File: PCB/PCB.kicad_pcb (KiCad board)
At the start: 2 copper layers, 95.2 x 61 mm, 47 parts, among them J1 Conn_01x02, J2 6P4C, J3 Conn_01x03, J4 Conn_02x08_Odd_Even, J5 Conn_01x08, J6 Conn_01x04, J7 Conn_02x03_Odd_Even, U1 LM358, U2 L293D

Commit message: PCB: Reattach vias to GND
Somewhere in the KiCad upgrade, it seems some vias got attached to
different nets. This manually fixes them.
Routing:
- net unconnected-(A1-~{RESET}-Pad1): vias 2 -> 0
- net unconnected-(A1-D13-Pad25): vias 1 -> 0
- net STRIP8: vias 2 -> 0
- net STRIP3: vias 1 -> 0
- net SCL: vias 1 -> 0
- net MOTION: vias 1 -> 0
- net GND: vias 102 -> 111
- net BRIDGE_IN_2: vias 1 -> 0
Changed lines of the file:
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@@
+	)
+	(via
+		(at 62.865 182.88)
+		(size 0.8)
+		(drill 0.4)
+		(layers "F.Cu" "B.Cu")
+		(net 3)
 	)
 	(via
@@
 	)
 	(via
+		(at 64.135 184.15)
+		(size 0.8)
+		(drill 0.4)
+		(layers "F.Cu" "B.Cu")
+		(net 3)
+	)
+	(via
 		(at 61.595 177.8)
 		(size 0.8)
@@
 	)
 	(via
+		(at 73.66 154.305)
+		(size 0.8)
+		(drill 0.4)
+		(layers "F.Cu" "B.Cu")
+		(free yes)
+		(net 3)
+	)
+	(via
 		(at 71.755 132.715)
 		(size 0.8)
@@
 	)
 	(via
+		(at 64.135 175.26)
+		(size 0.8)
+		(drill 0.4)
+		(layers "F.Cu" "B.Cu")
+		(net 3)
+	)
+	(via
 		(at 96.52 132.715)
 		(size 0.8)
@@
 	)
 	(via
+		(at 60.325 160.02)
+		(size 0.8)
+		(drill 0.4)
+		(layers "F.Cu" "B.Cu")
+		(net 3)
+	)
+	(via
 		(at 105.41 132.715)
 		(size 0.8)
@@
 	)
 	(via
+		(at 79.375 174.625)
+		(size 0.8)
+		(drill 0.4)
+		(layers "F.Cu" "B.Cu")
+		(net 3)
+	)
+	(via
 		(at 137.795 181.61)
 		(size 0.8)
@@
 	)
 	(via
+		(at 95.885 189.865)
+		(size 0.8)
+		(drill 0.4)
+		(layers "F.Cu" "B.Cu")
+		(net 3)
+	)
+	(via
 		(at 144.145 144.145)
 		(size 0.8)
@@
 	)
 	(via
+		(at 127.635 135.89)
+		(size 0.8)
+		(drill 0.4)
+		(layers "F.Cu" "B.Cu")
+		(net 3)
+	)
+	(via
 		(at 127.635 147.32)
 		(size 0.8)
@@
 	(via
 		(at 135.89 163.195)
+		(size 0.8)
+		(drill 0.4)
+		(layers "F.Cu" "B.Cu")
+		(net 3)
+	)
+	(via
+		(at 132.715 135.89)
 		(size 0.8)
 		(drill 0.4)
@@
 		(net 8)
 	)
-	(via
-		(at 79.375 174.625)
-		(size 0.8)
-		(drill 0.4)
-		(layers "F.Cu" "B.Cu")
-		(net 9)
-	)
 	(segment
 		(start 106.68 156.19)
@@
 		(net 10)
 	)
-	(via
-		(at 64.135 175.26)
-		(size 0.8)
-		(drill 0.4)
-		(layers "F.Cu" "B.Cu")
-		(net 10)
-	)
 	(segment
 		(start 113.03 178.64)
@@
 		(net 16)
 	)
-	(via
-		(at 127.635 135.89)
-		(size 0.8)
-		(drill 0.4)
-		(layers "F.Cu" "B.Cu")
-		(net 16)
-	)
-	(via
-		(at 62.865 182.88)
-		(size 0.8)
-		(drill 0.4)
-		(layers "F.Cu" "B.Cu")
-		(net 17)
-	)
-	(via
-		(at 64.135 184.15)
-		(size 0.8)
-		(drill 0.4)
-		(layers "F.Cu" "B.Cu")
-		(net 17)
-	)
 	(segment
 		(start 117.24 165.1)
@@
 		(net 35)
 	)
-	(via
-		(at 132.715 135.89)
-		(size 0.8)
-		(drill 0.4)
-		(layers "F.Cu" "B.Cu")
-		(net 35)
-	)
 	(segment
 		(start 76.2 182.88)
@@
 		(net 38)
 	)
-	(via
-		(at 73.66 154.305)
-		(size 0.8)
-		(drill 0.4)
-		(layers "F.Cu" "B.Cu")
-		(net 38)
-	)
 	(segment
 		(start 83.82 182.88)
@@
 		(net 43)
 	)
-	(via
-		(at 60.325 160.02)
-		(size 0.8)
-		(drill 0.4)
-		(layers "F.Cu" "B.Cu")
-		(net 43)
-	)
-	(via
-		(at 95.885 189.865)
-		(size 0.8)
-		(drill 0.4)
-		(layers "F.Cu" "B.Cu")
-		(net 43)
-	)

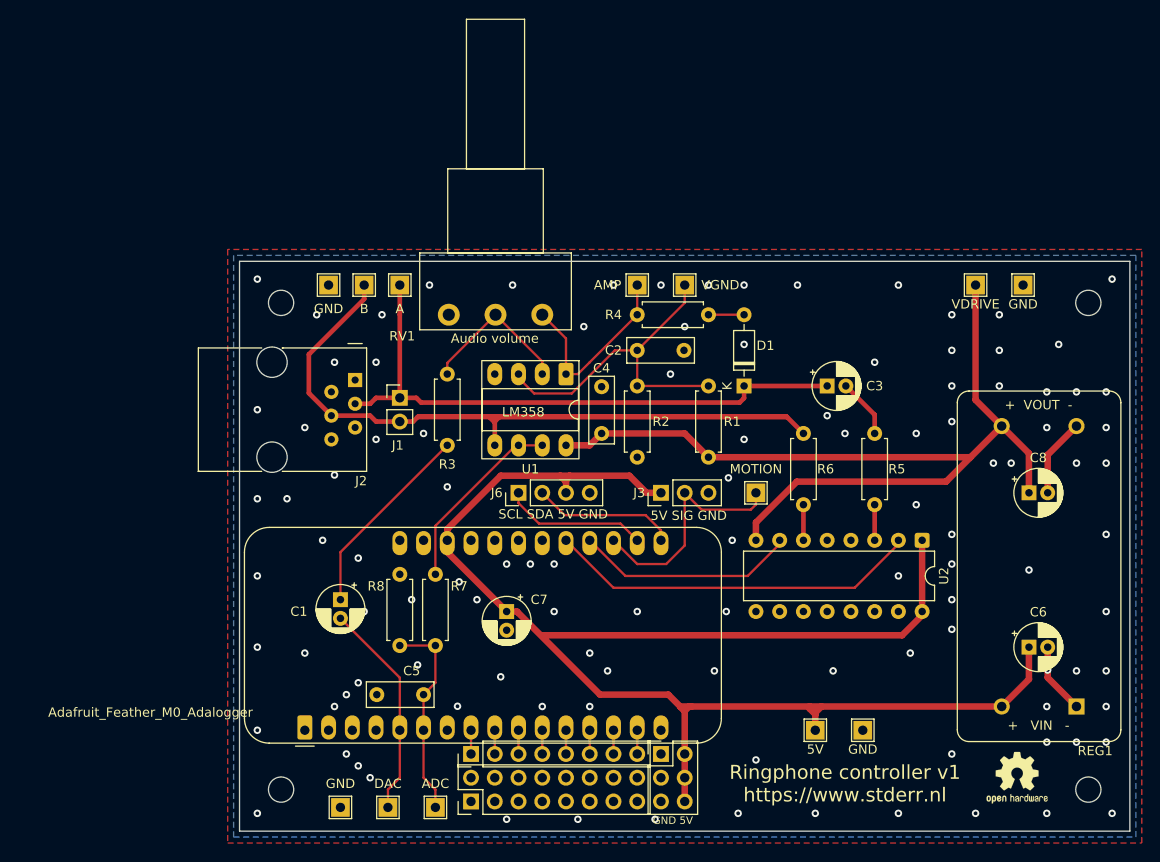
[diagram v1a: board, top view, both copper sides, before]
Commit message: PCB: Fix DRC errors
This updates a footprint, makes small layout changes and ignores some
violations.
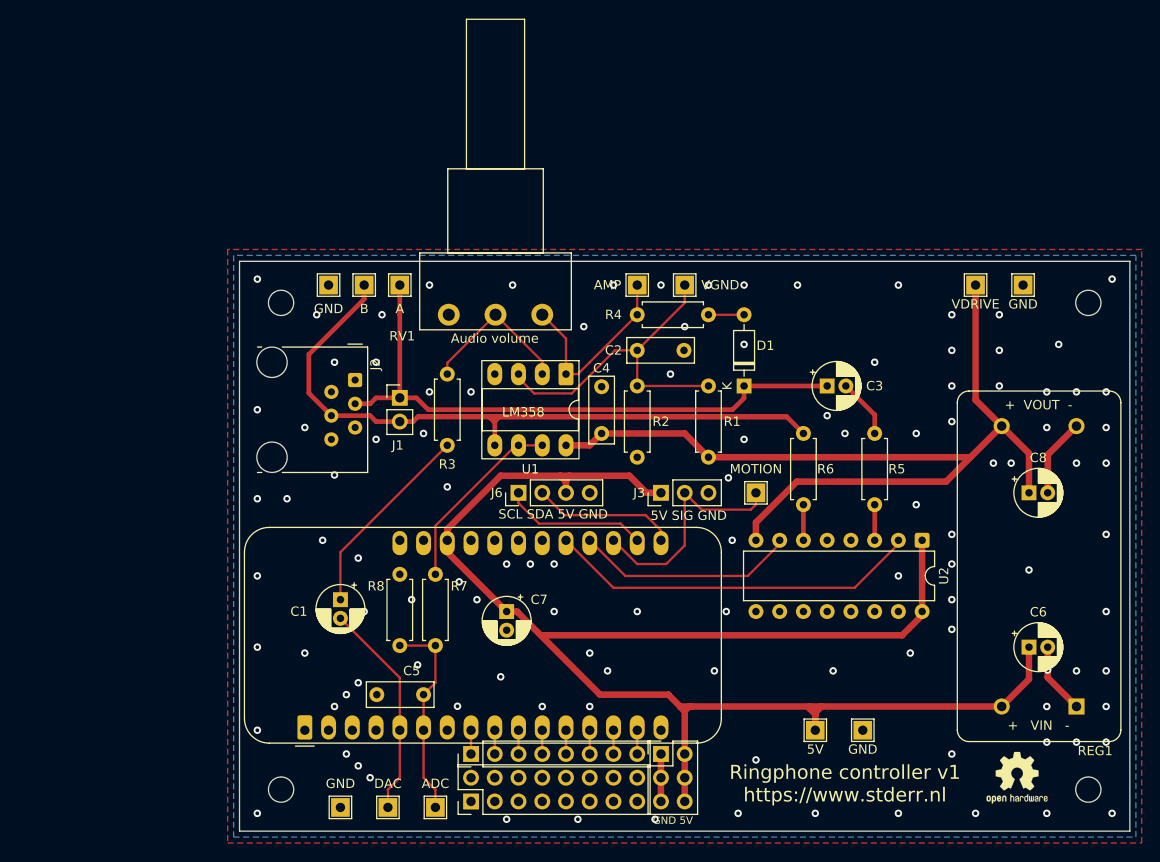
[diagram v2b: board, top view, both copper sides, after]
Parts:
- J2: footprint Connector_RJ:RJ12_Amphenol_54601 -> Connector_RJ:RJ12_Amphenol_54601-x06_Horizontal
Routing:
- net GND: track 16.0 -> 21.1 mm, vias 111 -> 113
- net TELEPHONE_A: track 64.5 -> 65.2 mm
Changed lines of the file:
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@@
 		)
 	)
-	(footprint "Connector_RJ:RJ12_Amphenol_54601"
+	(footprint "Connector_RJ:RJ12_Amphenol_54601-x06_Horizontal"
 		(layer "F.Cu")
 		(at 63.8 142.875 -90)
-		(descr "RJ12 connector  https://cdn.amphenol-icc.com/media/wysiwyg/files/drawing/c-bmj-0082.pdf")
+		(descr "RJ12 6P6C horizontal socket, plastic body, tab down, https://cdn.amphenol-icc.com/media/wysiwyg/files/drawing/c-bmj-0082.pdf")
 		(tags "RJ12 connector")
 		(property "Reference" "J2"
-			(at 10.795 -0.6398 180)
+			(at -1.66 -2.16 90)
 			(layer "F.SilkS")
 			(effects
@@
 		)
 		(property "Value" "6P4C"
-			(at 4.445 8.555 180)
+			(at 3.55 18.3 90)
 			(layer "F.Fab")
 			(effects
@@
 		(property "Datasheet" ""
 			(at 0 0 270)
+			(unlocked yes)
 			(layer "F.Fab")
 			(hide yes)
@@
 			)
 		)
-		(property "Description" "RJ connector, 6P6C (6 positions 6 connected), RJ12/RJ18/RJ25"
+		(property "Description" ""
 			(at 0 0 270)
+			(unlocked yes)
 			(layer "F.Fab")
 			(hide yes)
@@
 		(attr through_hole)
 		(fp_line
-			(start -3.43 16.77)
-			(end -3.43 9.99)
+			(start -3.53 10.45)
+			(end -3.53 9.99)
 			(stroke
 				(width 0.12)
@@
 		)
 		(fp_line
-			(start 9.77 16.77)
-			(end -3.43 16.77)
+			(start 9.89 10.45)
+			(end 9.89 9.99)
 			(stroke
 				(width 0.12)
@@
 		)
 		(fp_line
-			(start 9.77 16.77)
-			(end 9.77 9.99)
+			(start -3.53 7.79)
+			(end -3.53 -1.34)
 			(stroke
 				(width 0.12)
@@
 		)
 		(fp_line
-			(start 9.77 16.76)
-			(end 9.77 16.77)
+			(start -3.84 0.77)
+			(end -3.84 -0.76)
 			(stroke
-				(width 0.1)
+				(width 0.12)
 				(type solid)
 			)
@@
 		)
 		(fp_line
-			(start 9.77 16.65)
-			(end 9.77 16.77)
+			(start -3.53 -1.34)
+			(end 9.89 -1.34)
 			(stroke
-				(width 0.1)
+				(width 0.12)
 				(type solid)
 			)
@@
 		)
 		(fp_line
-			(start -3.43 7.79)
-			(end -3.43 -1.23)
+			(start 9.89 -1.34)
+			(end 9.89 7.79)
 			(stroke
 				(width 0.12)
@@
 		)
 		(fp_line
-			(start -3.43 7.72)
-			(end -3.43 7.79)
+			(start 10.28 17.27)
+			(end -3.92 17.27)
 			(stroke
-				(width 0.1)
+				(width 0.05)
 				(type solid)
 			)
-			(layer "F.SilkS")
+			(layer "F.CrtYd")
 		)
 		(fp_line
-			(start -3.9 0.77)
-			(end -3.9 -0.76)
+			(start -4.03 9.64)
+			(end -3.92 9.64)
 			(stroke
-				(width 0.12)
-				(type solid)
+				(width 0.05)
+				(type default)
 			)
-			(layer "F.SilkS")
+			(layer "F.CrtYd")
 		)
 		(fp_line
-			(start -3.43 -1.23)
-			(end 9.77 -1.23)
+			(start -3.92 9.64)
+			(end -3.92 17.27)
 			(stroke
-				(width 0.12)
+				(width 0.05)
 				(type solid)
 			)
-			(layer "F.SilkS")
+			(layer "F.CrtYd")
 		)
 		(fp_line
-			(start 9.77 -1.23)
-			(end 9.77 7.79)
+			(start 10.28 9.64)
+			(end 10.28 17.27)
 			(stroke
-				(width 0.12)
+				(width 0.05)
 				(type solid)
 			)
-			(layer "F.SilkS")
+			(layer "F.CrtYd")
 		)
 		(fp_line
-			(start -4.04 17.27)
-			(end -4.04 -1.73)
+			(start 10.39 9.64)
+			(end 10.28 9.64)
 			(stroke
 				(width 0.05)
-				(type solid)
+				(type default)
+			)
+			(layer "F.CrtYd")
+		)
+		(fp_line
+			(start -4.03 8.14)
+			(end -4.03 9.64)
+			(stroke
+				(width 0.05)
+				(type default)
+			)
+			(layer "F.CrtYd")
+		)
+		(fp_line
+			(start -4.03 8.14)
+			(end -3.92 8.14)
+			(stroke
+				(width 0.05)
+				(type default)
 			)
 			(layer "F.CrtYd")
 		)
 		(fp_line
-			(start 10.38 17.27)
-			(end -4.04 17.27)
+			(start 10.39 8.14)
+			(end 10.39 9.64)
+			(stroke
+				(width 0.05)
+				(type default)
+			)
+			(layer "F.CrtYd")
+		)
+		(fp_line
+			(start 10.39 8.14)
+			(end 10.28 8.14)
+			(stroke
+				(width 0.05)
+				(type default)
+			)
+			(layer "F.CrtYd")
+		)
+		(fp_line
+			(start -3.92 -1.73)
+			(end -3.92 8.14)
 			(stroke
 				(width 0.05)
@@
 		)
 		(fp_line
-			(start -4.04 -1.73)
-			(end 10.38 -1.73)
+			(start -3.92 -1.73)
+			(end 10.28 -1.73)
 			(stroke
 				(width 0.05)
@@
 		)
 		(fp_line
-			(start 10.38 -1.73)
-			(end 10.38 17.27)
+			(start 10.28 -1.73)
+			(end 10.28 8.14)
 			(stroke
 				(width 0.05)
@@
 		)
 		(fp_line
-			(start -3.43 16.77)
-			(end -3.43 0.52)
+			(start -3.42 16.77)
+			(end -3.42 0.52)
 			(stroke
 				(width 0.1)
@@
 		)
 		(fp_line
-			(start 9.77 16.77)
-			(end -3.43 16.77)
+			(start 9.78 16.77)
+			(end -3.42 16.77)
 			(stroke
 				(width 0.1)
@@
 		)
 		(fp_line
-			(start -3.43 0.52)
-			(end -2.93 0.02)
+			(start -3.42 0.52)
+			(end -2.92 0.02)
 			(stroke
 				(width 0.1)
@@
 		)
 		(fp_line
-			(start -2.93 0.02)
-			(end -3.43 -0.48)
+			(start -2.92 0.02)
+			(end -3.42 -0.48)
 			(stroke
 				(width 0.1)
@@
 		)
 		(fp_line
-			(start -3.43 -0.48)
-			(end -3.43 -1.23)
+			(start -3.42 -0.48)
+			(end -3.42 -1.23)
 			(stroke
 				(width 0.1)
@@
 		)
 		(fp_line
-			(start -3.43 -1.23)
-			(end 9.77 -1.23)
+			(start -3.42 -1.23)
+			(end 9.78 -1.23)
 			(stroke
 				(width 0.1)
@@
 		)
 		(fp_line
-			(start 9.77 -1.23)
-			(end 9.77 16.77)
+			(start 9.78 -1.23)
+			(end 9.78 16.77)
 			(stroke
 				(width 0.1)
@@
 		)
 		(fp_text user "${REFERENCE}"
-			(at 2.54 8.555 180)
+			(at 3.18 7.77 0)
 			(layer "F.Fab")
 			(effects
@@
 		)
 		(pad "" np_thru_hole circle
-			(at -1.91 8.89 270)
+			(at -1.9 8.89 270)
 			(size 3.25 3.25)
 			(drill 3.25)
@@
 		)
 		(pad "" np_thru_hole circle
-			(at 8.25 8.89 270)
+			(at 8.26 8.89 270)
 			(size 3.25 3.25)
 			(drill 3.25)
 			(layers "*.Cu" "*.Mask")
 		)
-		(pad "1" thru_hole rect
+		(pad "1" thru_hole roundrect
 			(at 0 0 270)
 			(size 1.52 1.52)
@@
 			(layers "*.Cu" "*.Mask")
 			(remove_unused_layers no)
+			(roundrect_rratio 0.1644736842)
 			(net 28 "unconnected-(J2-Pad1)")
 			(pintype "passive+no_connect")
@@
 		)
 		(embedded_fonts no)
-		(model "${KISYS3DMOD}/Connector_RJ.3dshapes/RJ12_Amphenol_54601.wrl"
+		(model "${KICAD9_3DMODEL_DIR}/Connector_RJ.3dshapes/RJ12_Amphenol_54601-x06_Horizontal.wrl"
 			(offset
 				(xyz 0 0 0)
@@
 			(at 1.905 -16.51 0)
 			(layer "F.SilkS")
+			(hide yes)
 			(effects
 				(font
@@
 		(sheetname "/")
 		(sheetfile "PCB.kicad_sch")
-		(attr exclude_from_pos_files)
+		(attr exclude_from_pos_files allow_missing_courtyard)
 		(fp_poly
 			(pts
@@
 	)
 	(segment
+		(start 96.52 182.88)
+		(end 96.52 185.42)
+		(width 0.7)
+		(layer "F.Cu")
+		(net 3)
+	)
+	(segment
+		(start 96.52 185.42)
+		(end 96.52 187.96)
+		(width 0.7)
+		(layer "F.Cu")
+		(net 3)
+	)
+	(segment
 		(start 137.89 154.94)
 		(end 137.89 151.504399)
@@
 	)
 	(via
+		(at 71.755 144.145)
+		(size 0.8)
+		(drill 0.4)
+		(layers "F.Cu" "B.Cu")
+		(free yes)
+		(net 3)
+	)
+	(via
 		(at 127.635 143.51)
 		(size 0.8)
@@
 	)
 	(via
+		(at 76.2 144.145)
+		(size 0.8)
+		(drill 0.4)
+		(layers "F.Cu" "B.Cu")
+		(free yes)
+		(net 3)
+	)
+	(via
 		(at 137.795 177.8)
 		(size 0.8)
@@
 	)
 	(segment
-		(start 65.405 145.415)
-		(end 63.8 145.415)
+		(start 104.17 146.05)
+		(end 71.62 146.05)
 		(width 0.5)
 		(layer "F.Cu")
@@
 	)
 	(segment
-		(start 66.04 144.78)
-		(end 65.405 145.415)
+		(start 105.41 143.51)
+		(end 105.41 144.81)
 		(width 0.5)
 		(layer "F.Cu")
@@
 	)
 	(segment
-		(start 104.932 145.288)
-		(end 70.858 145.288)
+		(start 65.405 145.415)
+		(end 63.8 145.415)
 		(width 0.5)
 		(layer "F.Cu")
@@
 	)
 	(segment
-		(start 68.58 135.89)
-		(end 68.58 144.78)
+		(start 66.04 144.78)
+		(end 65.405 145.415)
 		(width 0.5)
 		(layer "F.Cu")
@@
 	)
 	(segment
-		(start 105.41 143.51)
-		(end 105.41 144.81)
+		(start 105.41 144.81)
+		(end 104.17 146.05)
 		(width 0.5)
 		(layer "F.Cu")
@@
 	)
 	(segment
-		(start 114.3 143.51)
-		(end 105.41 143.51)
+		(start 68.58 135.89)
+		(end 68.58 144.78)
 		(width 0.5)
 		(layer "F.Cu")
@@
 	)
 	(segment
-		(start 70.35 144.78)
-		(end 70.858 145.288)
+		(start 114.3 143.51)
+		(end 105.41 143.51)
 		(width 0.5)
 		(layer "F.Cu")
@@
 	)
 	(segment
-		(start 68.58 132.715)
-		(end 68.58 135.89)
+		(start 71.62 146.05)
+		(end 70.35 144.78)
 		(width 0.5)
 		(layer "F.Cu")
@@
 	)
 	(segment
-		(start 68.58 144.78)
-		(end 70.35 144.78)
+		(start 68.58 132.715)
+		(end 68.58 135.89)
 		(width 0.5)
 		(layer "F.Cu")
@@
 	)
 	(segment
-		(start 105.41 144.81)
-		(end 104.932 145.288)
+		(start 70.35 144.78)
+		(end 68.58 144.78)
 		(width 0.5)
 		(layer "F.Cu")

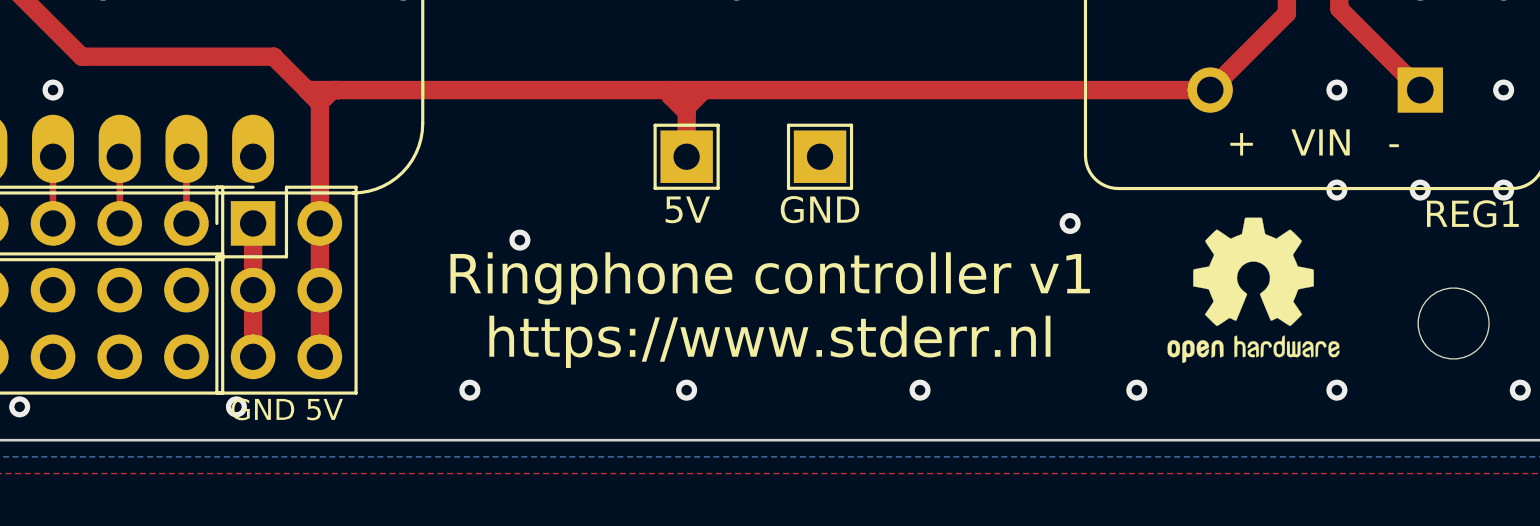
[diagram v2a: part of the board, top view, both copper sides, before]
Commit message: Setup PCB-workflows automation
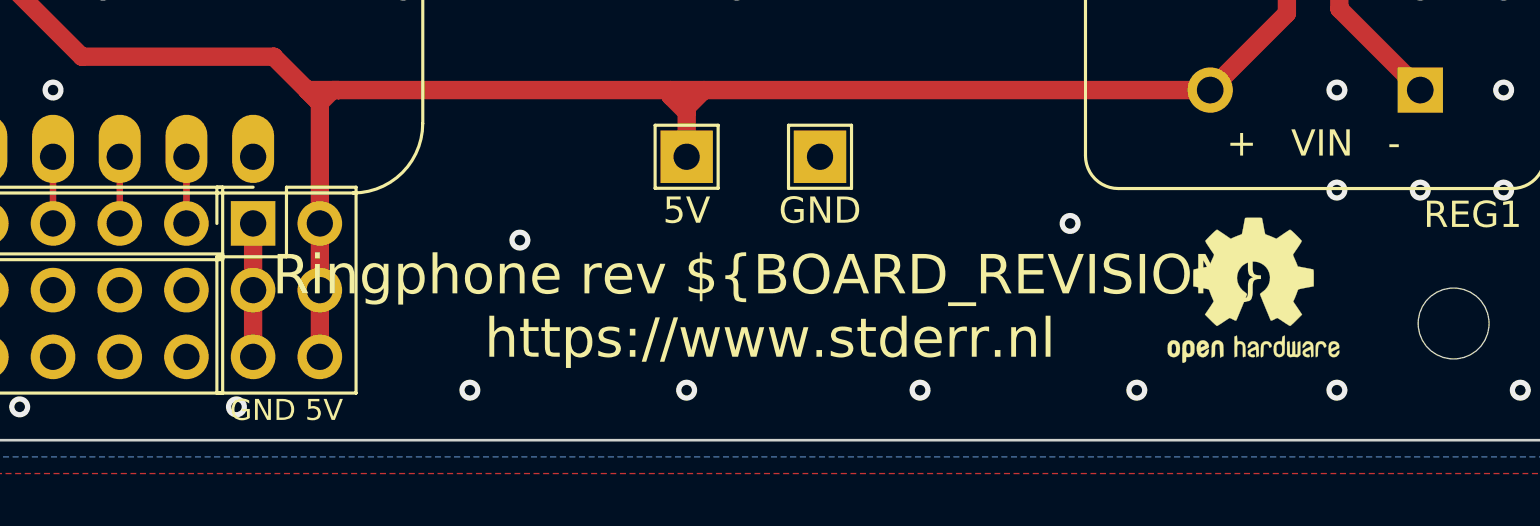
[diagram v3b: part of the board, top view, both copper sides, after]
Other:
- board text added: "Ringphone rev ${BOARD_REVISION} https://www.stderr.nl"
- board text removed: "Ringphone controller v1 https://www.stderr.nl"
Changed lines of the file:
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@@
 		)
 	)
-	(gr_text "Ringphone controller v1\nhttps://www.stderr.nl"
+	(gr_text "Ringphone rev ${BOARD_REVISION}\nhttps://www.stderr.nl"
 		(at 116.205 186.055 0)
 		(layer "F.SilkS")

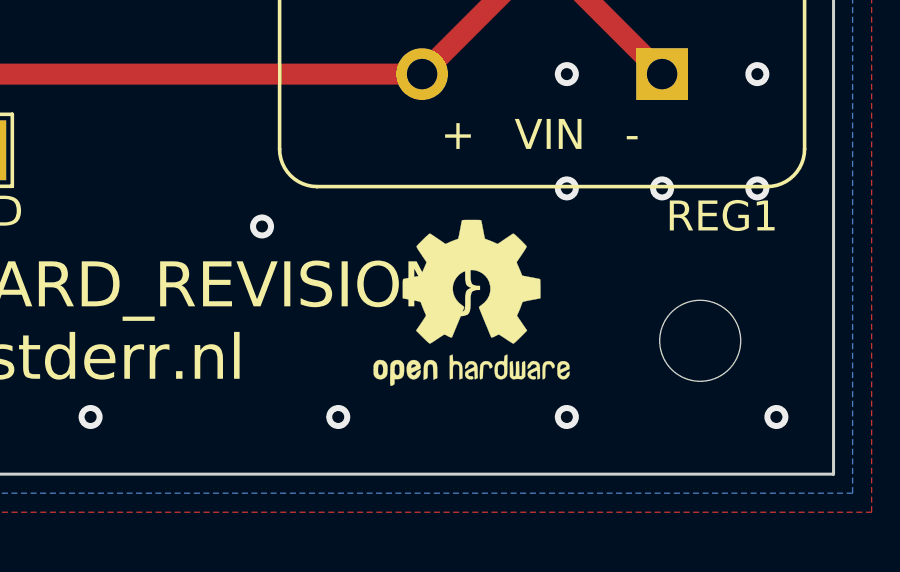
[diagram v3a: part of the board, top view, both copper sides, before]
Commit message: Update license info, switch to CERN-OHL-P v2
This also puts the licens on the silkscreen.
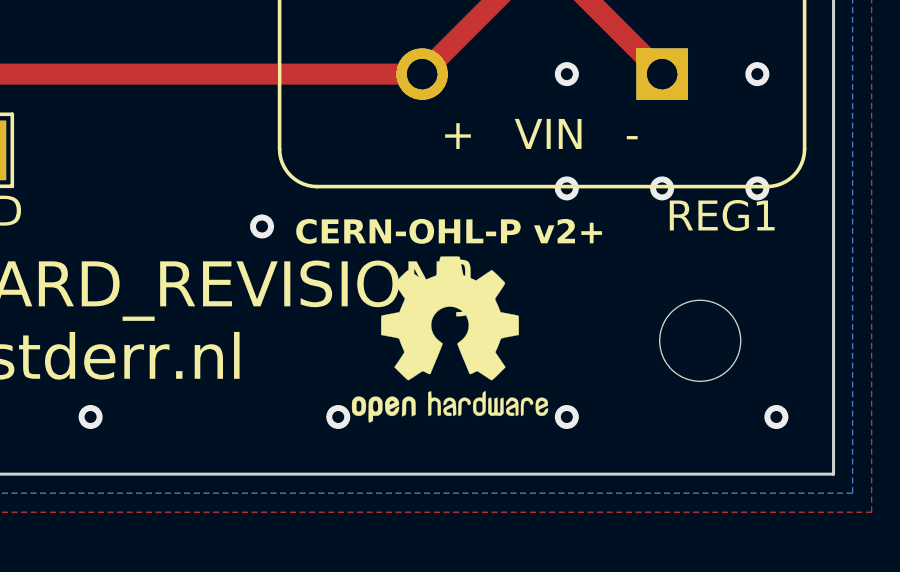
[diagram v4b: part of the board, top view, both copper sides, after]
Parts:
- moved LOGO1 1.42 mm to (133.9, 186.6)
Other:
- board text added: "CERN-OHL-P v2+"
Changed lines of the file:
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@@
 	)
 	(paper "A4")
+	(title_block
+		(title "Ringphone controller")
+		(company "https://www.stderr.nl")
+		(comment 2 "CERN Open Hardware Licence v2 - Permissive")
+	)
 	(layers
 		(0 "F.Cu" signal)
@@
 	(footprint "Symbol:OSHW-Logo2_7.3x6mm_SilkScreen"
 		(layer "F.Cu")
-		(at 134.62 185.42)
+		(at 133.9 186.64)
 		(descr "Open Source Hardware Symbol")
 		(tags "Logo Symbol OSHW")
@@
 		)
 	)
+	(gr_text "CERN-OHL-P v2+"
+		(at 133.9 183.54 0)
+		(layer "F.SilkS")
+		(effects
+			(font
+				(size 0.8 0.8)
+				(thickness 0.16)
+				(bold yes)
+			)
+			(justify bottom)
+		)
+	)
